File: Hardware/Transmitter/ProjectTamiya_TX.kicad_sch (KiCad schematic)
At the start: 40 parts, among them J1 Boot, J10 NRF, J2 Power, J3 Serial, J4 Steering, J5 Throttle, J6 ENC1, J7 OLED, J8 ENC2, J9 Debug, Q1 RYC002N05T316, Q2 RYC002N05T316, Q3 RYC002N05T316, SW1 Reset, SW2 Switch, U1 STM32F303CCT6, U2 AP2111H-3.3TRG1, Y1 LFXTAL063189 [15pF]

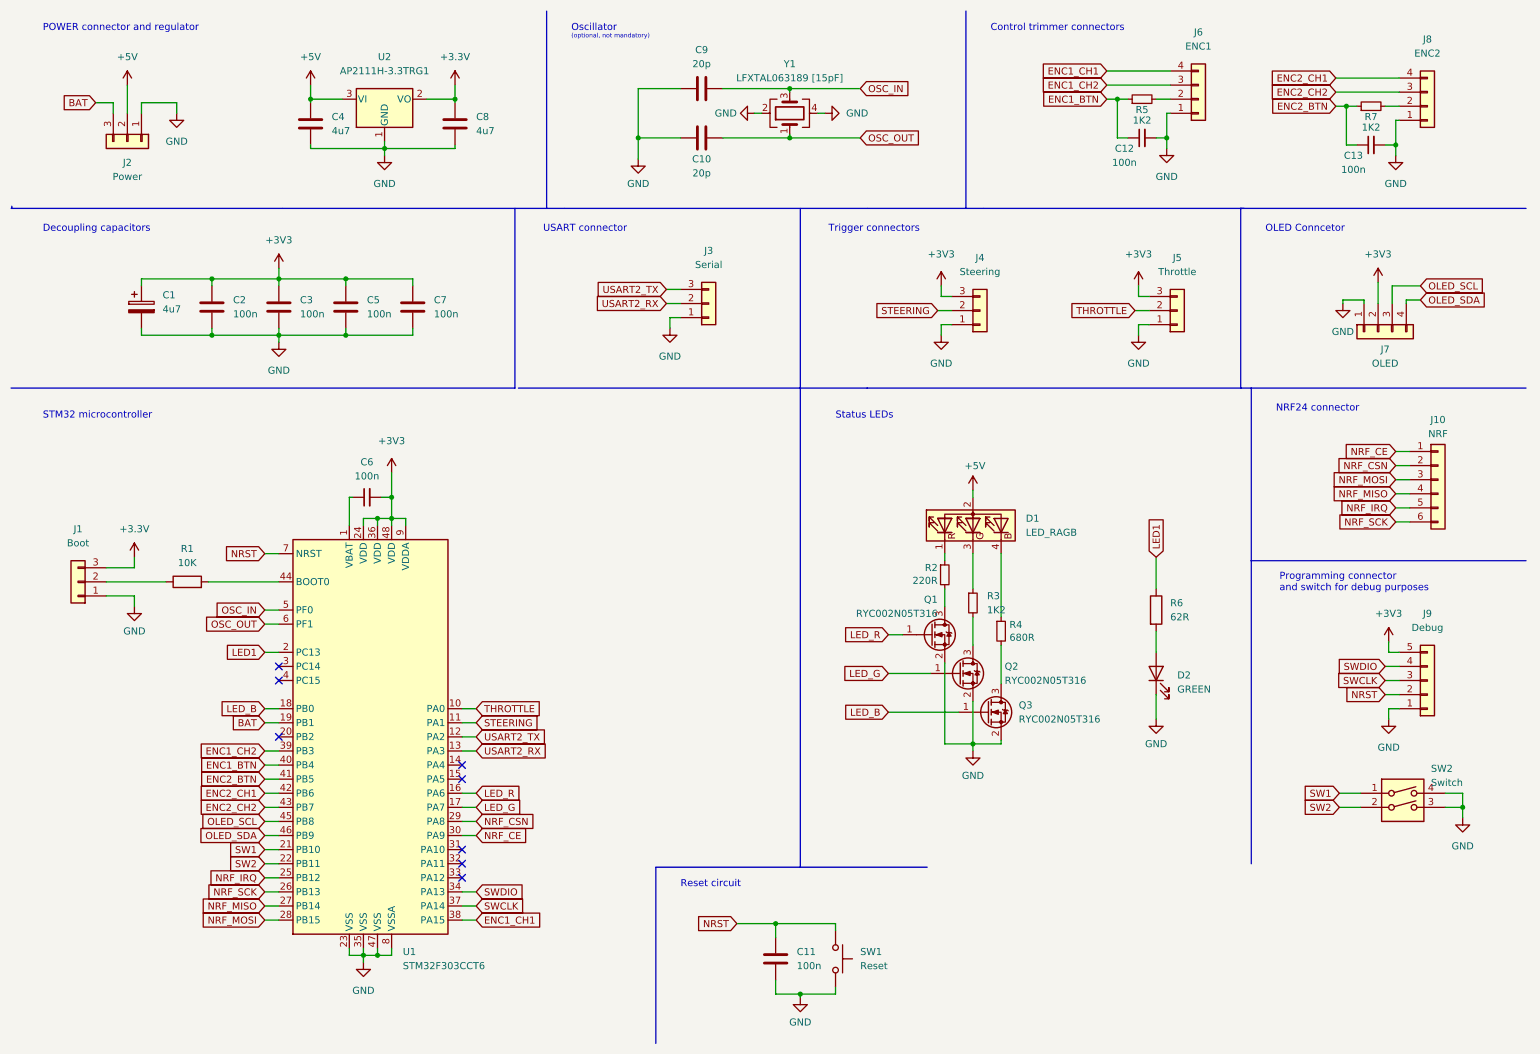
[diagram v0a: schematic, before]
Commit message: Small schematics adjustments
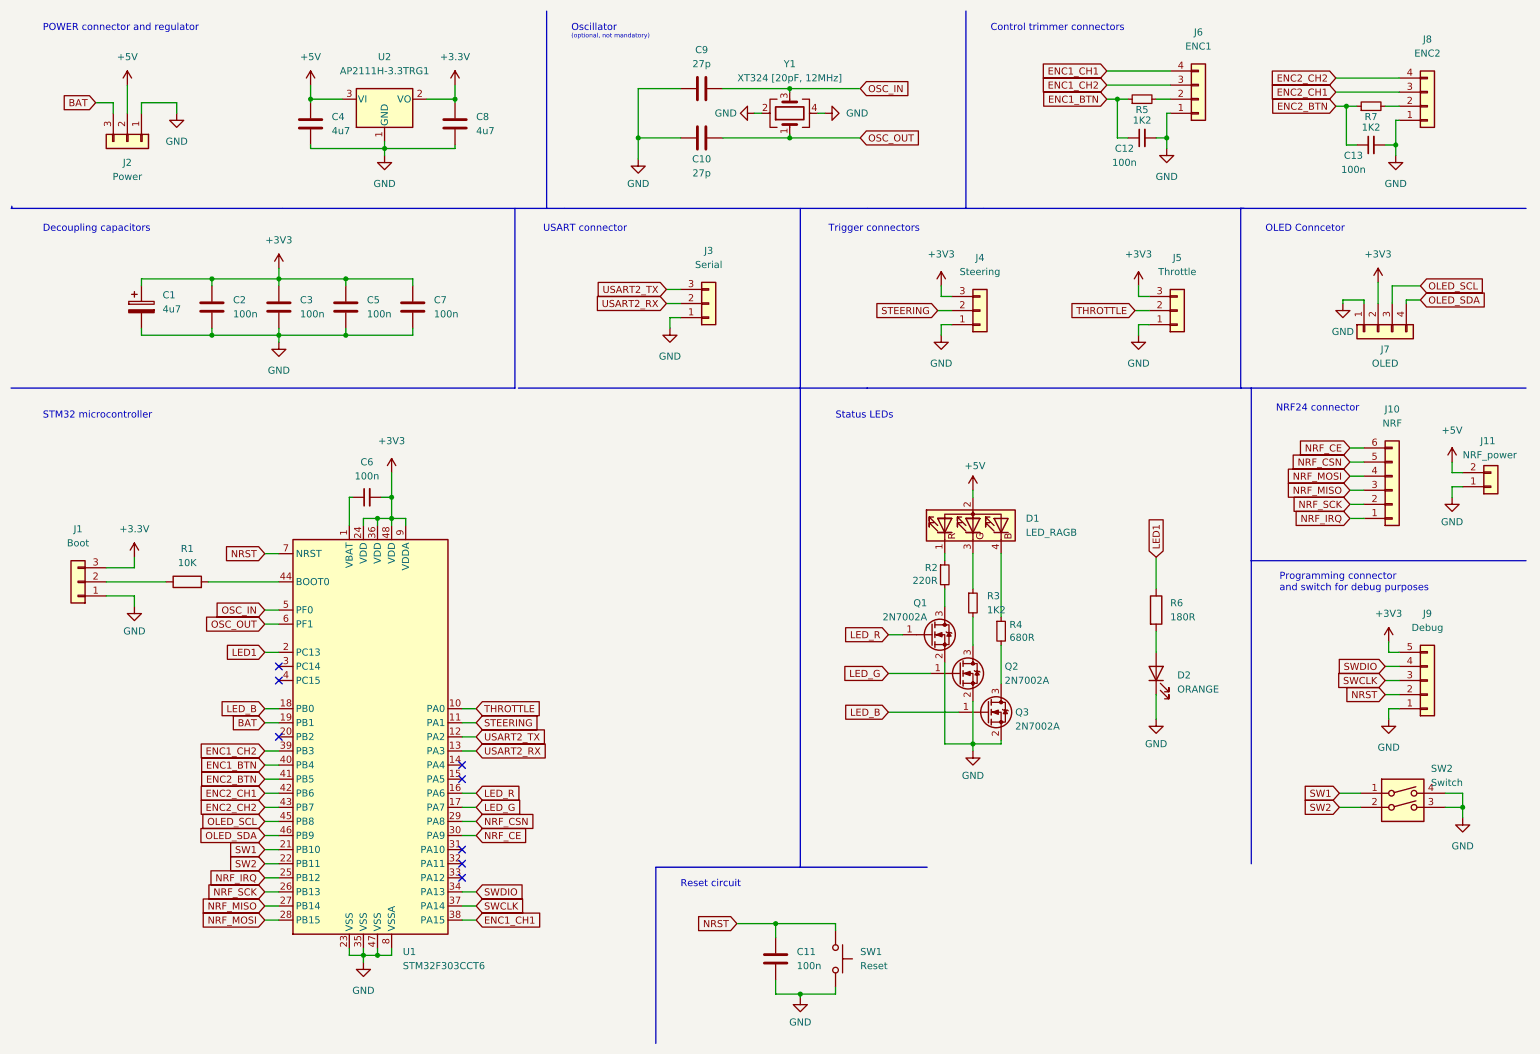
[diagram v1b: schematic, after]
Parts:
- removed Q1, Q2, Q3: RYC002N05T316, Package_TO_SOT_SMD:SOT-23, symbol Device:Q_NMOS_GSD
- added J11: NRF_power, Connector_Wire:SolderWire-0.25sqmm_1x02_P4.2mm_D0.65mm_OD1.7mm_Relief, symbol Connector_Generic:Conn_01x02
- added Q1, Q2, Q3: 2N7002A, Package_TO_SOT_SMD:SOT-23, symbol Transistor_FET:2N7002
- C10, C9: value 20p -> 27p
- D2: value GREEN -> ORANGE
- J10: footprint Connector_Wire:SolderWire-0.25sqmm_1x06_P4.2mm_D0.65mm_OD1.7mm_Relief -> Connector_Wire:SolderWire-0.15sqmm_1x06_P4mm_D0.5mm_OD1.5mm_Relief
- J7: footprint Connector_PinSocket_2.54mm:PinSocket_1x04_P2.54mm_Vertical -> Connector_PinSocket_2.54mm:PinSocket_1x04_P2.54mm_Vertical_SMD_Pin1Left
- R2, R3, R4: footprint Resistor_SMD:R_0603_1608Metric_Pad0.98x0.95mm_HandSolder -> Resistor_THT:R_Axial_DIN0204_L3.6mm_D1.6mm_P2.54mm_Vertical
- R6: value 62R -> 180R
- Y1: value LFXTAL063189 [15pF] -> XT324 [20pF, 12MHz]; footprint Crystal:Crystal_SMD_5032-4Pin_5.0x3.2mm -> Crystal:Crystal_SMD_3225-4Pin_3.2x2.5mm_HandSoldering
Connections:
- net +5V: now also J11.2 (Pin_2)
- net ENC2_CH1: now also J8.3 (Pin_3); no longer J8.4 (Pin_4)
- net ENC2_CH2: now also J8.4 (Pin_4); no longer J8.3 (Pin_3)
- net GND: now also J11.1 (Pin_1), Q1.2 (S), Q2.2 (S), Q3.2 (S)
- net LED_B: now also Q3.1 (G)
- net LED_G: now also Q2.1 (G)
- net LED_R: now also Q1.1 (G)
- net NRF_CE: now also J10.6 (Pin_6); no longer J10.1 (Pin_1)
- net NRF_CSN: now also J10.5 (Pin_5); no longer J10.2 (Pin_2)
- net NRF_IRQ: now also J10.1 (Pin_1); no longer J10.5 (Pin_5)
- net NRF_MISO: now also J10.3 (Pin_3); no longer J10.4 (Pin_4)
- net NRF_MOSI: now also J10.4 (Pin_4); no longer J10.3 (Pin_3)
- net NRF_SCK: now also J10.2 (Pin_2); no longer J10.6 (Pin_6)
- net at R3.2: now also Q2.3 (D)
- net at R4.2: now also Q3.3 (D)
- net at R2.2: now also Q1.3 (D)
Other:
- title: ProjectTamiya - Transmitter schematics -> ProjectTamiya - Transmitter
- moved on the sheet: J10

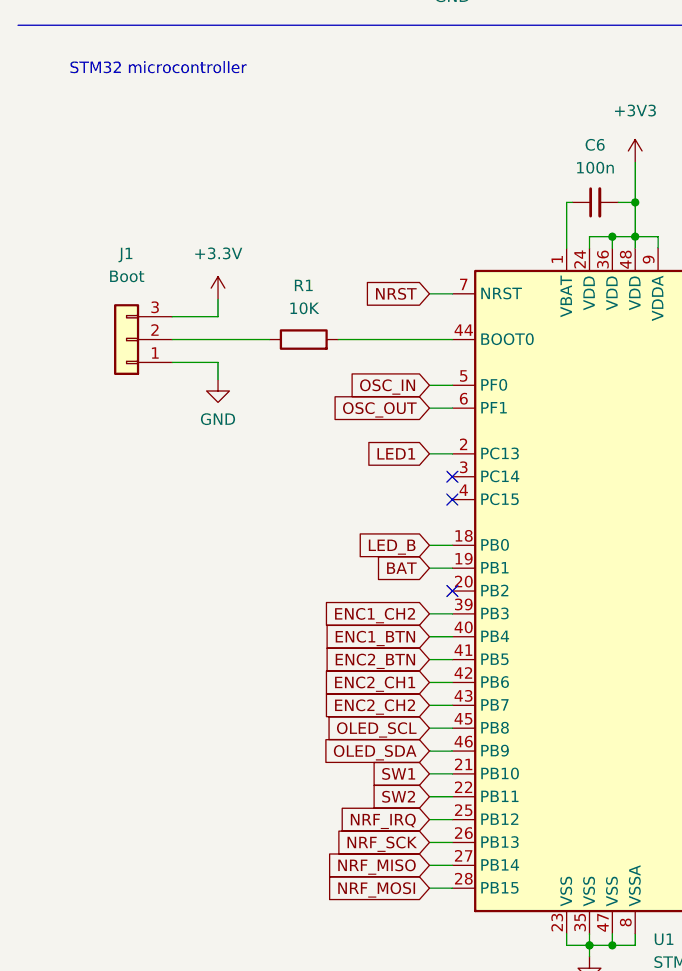
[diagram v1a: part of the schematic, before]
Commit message: Switch pin assignment change, updated schematics, complete PCB
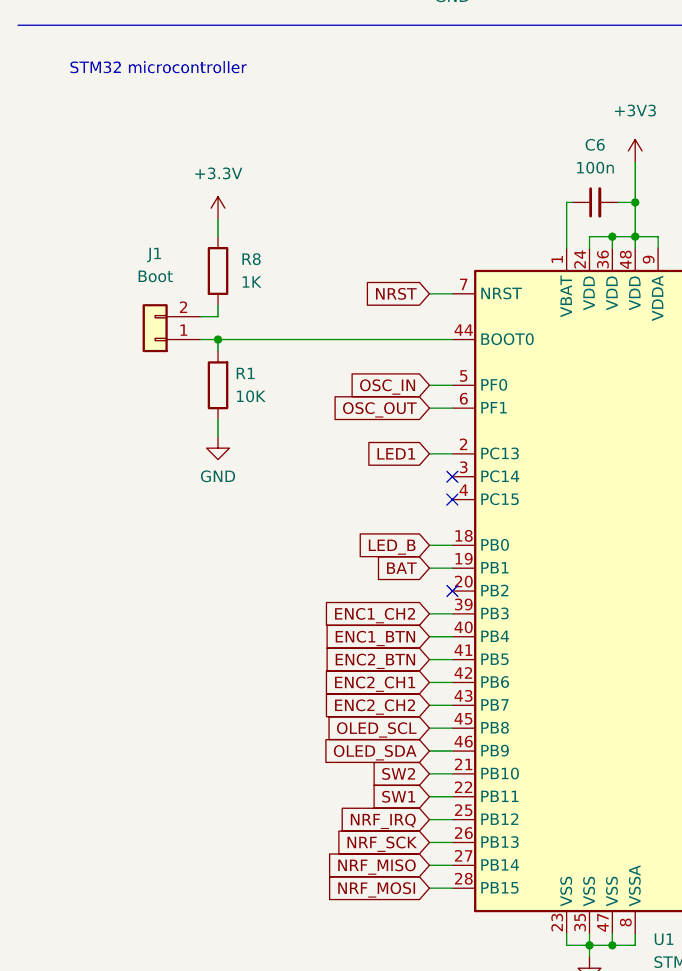
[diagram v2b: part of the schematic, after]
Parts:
- removed J1: Boot, Connector_PinHeader_2.54mm:PinHeader_1x03_P2.54mm_Vertical, symbol Connector_Generic:Conn_01x03
- added J1: Boot, Connector_PinHeader_2.54mm:PinHeader_1x02_P2.54mm_Vertical, symbol Connector_Generic:Conn_01x02
- added R8: 1K, Resistor_SMD:R_0603_1608Metric_Pad0.98x0.95mm_HandSolder, symbol Device:R
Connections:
- net +3V3: now also R8.1
- net GND: now also R1.1
- net SW1: now also U1.22 (PB11); no longer U1.21 (PB10)
- net SW2: now also U1.21 (PB10); no longer U1.22 (PB11)
- net at R1.2, U1.44 (BOOT0): now also J1.1 (Pin_1)
- new net: J1.2 (Pin_2), R8.2
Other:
- moved on the sheet: R1

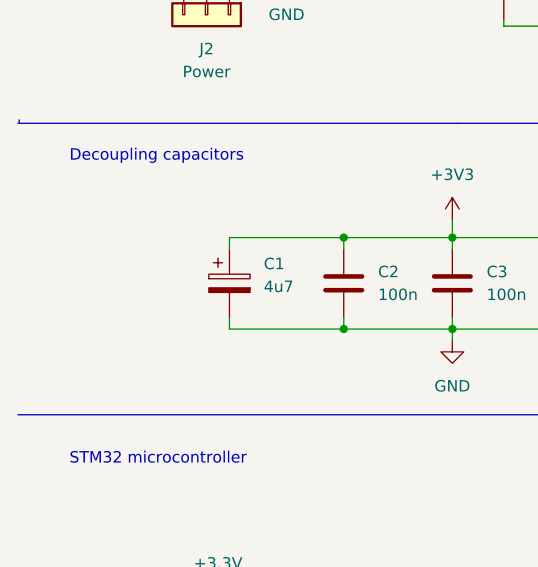
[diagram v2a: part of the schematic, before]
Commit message: Small PCB routing changes, silkscreen improvements
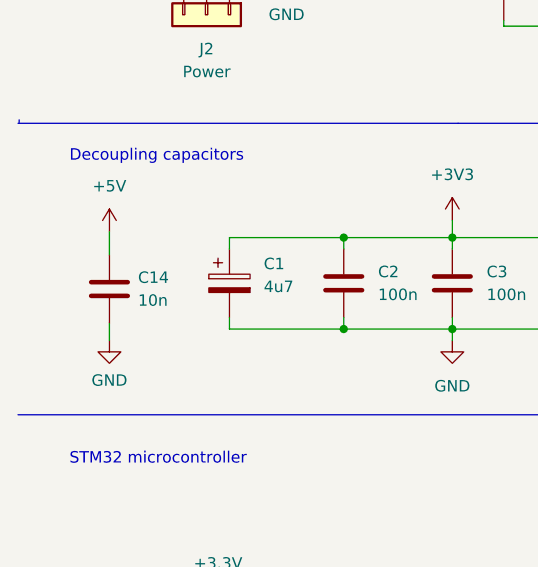
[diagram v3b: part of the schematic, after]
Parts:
- added C14: 10n, Capacitor_SMD:C_0603_1608Metric_Pad1.08x0.95mm_HandSolder, symbol Device:C
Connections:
- net +5V: now also C14.1
- net GND: now also C14.2
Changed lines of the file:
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@@
+    (stroke (width 0) (type default) (color 0 0 0 0))
+  )
+  (wire (pts (xy 22.225 69.85) (xy 22.225 71.755))
     (stroke (width 0) (type default) (color 0 0 0 0))
   )
@@
   )
   (wire (pts (xy 84.455 70.485) (xy 84.455 69.215))
+    (stroke (width 0) (type default) (color 0 0 0 0))
+  )
+  (wire (pts (xy 22.225 59.69) (xy 22.225 62.23))
     (stroke (width 0) (type default) (color 0 0 0 0))
   )
@@
     (pin "5")
   )
+  (symbol (lib_id "power:+5V") (at 22.225 59.69 0) (unit 1)
+    (in_bom yes) (on_board yes) (fields_autoplaced)
+    (property "Reference" "#PWR033" (id 0) (at 22.225 63.5 0)
+      (effects (font (size 1.27 1.27)) hide)
+    )
+    (property "Value" "+5V" (id 1) (at 22.225 54.61 0))
+    (property "Footprint" "" (id 2) (at 22.225 59.69 0)
+      (effects (font (size 1.27 1.27)) hide)
+    )
+    (property "Datasheet" "" (id 3) (at 22.225 59.69 0)
+      (effects (font (size 1.27 1.27)) hide)
+    )
+    (pin "1")
+  )
   (symbol (lib_id "Device:C") (at 60.325 65.405 0) (unit 1)
     (in_bom yes) (on_board yes) (fields_autoplaced)
@@
     (pin "1")
   )
+  (symbol (lib_id "Device:C") (at 22.225 66.04 0) (unit 1)
+    (in_bom yes) (on_board yes) (fields_autoplaced)
+    (property "Reference" "C14" (id 0) (at 25.4 64.7699 0)
+      (effects (font (size 1.27 1.27)) (justify left))
+    )
+    (property "Value" "10n" (id 1) (at 25.4 67.3099 0)
+      (effects (font (size 1.27 1.27)) (justify left))
+    )
+    (property "Footprint" "Capacitor_SMD:C_0603_1608Metric_Pad1.08x0.95mm_HandSolder" (id 2) (at 23.1902 69.85 0)
+      (effects (font (size 1.27 1.27)) hide)
+    )
+    (property "Datasheet" "~" (id 3) (at 22.225 66.04 0)
+      (effects (font (size 1.27 1.27)) hide)
+    )
+    (pin "1")
+    (pin "2")
+  )
   (symbol (lib_id "power:+3V3") (at 179.705 61.595 0) (unit 1)
     (in_bom yes) (on_board yes) (fields_autoplaced)
@@
     (pin "3")
     (pin "4")
+  )
+  (symbol (lib_id "power:GND") (at 22.225 71.755 0) (unit 1)
+    (in_bom yes) (on_board yes) (fields_autoplaced)
+    (property "Reference" "#PWR034" (id 0) (at 22.225 78.105 0)
+      (effects (font (size 1.27 1.27)) hide)
+    )
+    (property "Value" "GND" (id 1) (at 22.225 76.2 0))
+    (property "Footprint" "" (id 2) (at 22.225 71.755 0)
+      (effects (font (size 1.27 1.27)) hide)
+    )
+    (property "Datasheet" "" (id 3) (at 22.225 71.755 0)
+      (effects (font (size 1.27 1.27)) hide)
+    )
+    (pin "1")
   )
   (symbol (lib_id "power:+5V") (at 271.78 93.345 0) (unit 1)
@@
       (reference "#PWR032") (unit 1) (value "GND") (footprint "")
     )
+    (path "/b51343d5-5258-4bf6-a38b-315156655fe7"
+      (reference "#PWR033") (unit 1) (value "+5V") (footprint "")
+    )
+    (path "/fc2e6937-75ad-4c5e-862d-3bdf44129aa7"
+      (reference "#PWR034") (unit 1) (value "GND") (footprint "")
+    )
     (path "/4088a0a9-236b-4b9b-a260-6083e64fab90"
       (reference "C1") (unit 1) (value "4u7") (footprint "Capacitor_Tantalum_SMD:CP_EIA-1608-10_AVX-L_Pad1.25x1.05mm_HandSolder")
@@
       (reference "C13") (unit 1) (value "100n") (footprint "Capacitor_SMD:C_0603_1608Metric_Pad1.08x0.95mm_HandSolder")
     )
+    (path "/c3f4e4fd-33f7-404b-a4b5-b1fa76c627d6"
+      (reference "C14") (unit 1) (value "10n") (footprint "Capacitor_SMD:C_0603_1608Metric_Pad1.08x0.95mm_HandSolder")
+    )
     (path "/9a0eb21d-73ee-4fea-bf1f-59fce775cdc8"

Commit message: Final checkup and small adjustments
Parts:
- Q1, Q2, Q3: value 2N7002A -> 2N7002BK
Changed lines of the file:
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@@
       (effects (font (size 1.27 1.27)) (justify left))
     )
-    (property "Value" "2N7002A" (id 1) (at 191.135 132.715 0)
+    (property "Value" "2N7002BK" (id 1) (at 191.135 132.715 0)
       (effects (font (size 1.27 1.27)) (justify left))
     )
@@
       (effects (font (size 1.27 1.27)) (justify right))
     )
-    (property "Value" "2N7002A" (id 1) (at 177.165 121.285 0)
+    (property "Value" "2N7002BK" (id 1) (at 177.165 121.285 0)
       (effects (font (size 1.27 1.27)) (justify right))
     )
@@
       (effects (font (size 1.27 1.27)) (justify left))
     )
-    (property "Value" "2N7002A" (id 1) (at 193.04 140.97 0)
+    (property "Value" "2N7002BK" (id 1) (at 193.04 140.97 0)
       (effects (font (size 1.27 1.27)) (justify left))
     )
@@
     )
     (path "/4a4d9b9b-c50f-4ef0-8277-cdd97ceed0a6"
-      (reference "Q1") (unit 1) (value "2N7002A") (footprint "Package_TO_SOT_SMD:SOT-23")
+      (reference "Q1") (unit 1) (value "2N7002BK") (footprint "Package_TO_SOT_SMD:SOT-23")
     )
     (path "/2bb276a7-8ab2-4be3-9b32-a7ea311015c9"
-      (reference "Q2") (unit 1) (value "2N7002A") (footprint "Package_TO_SOT_SMD:SOT-23")
+      (reference "Q2") (unit 1) (value "2N7002BK") (footprint "Package_TO_SOT_SMD:SOT-23")
     )
     (path "/9cd35799-ec18-4e90-9608-c6514838a377"
-      (reference "Q3") (unit 1) (value "2N7002A") (footprint "Package_TO_SOT_SMD:SOT-23")
+      (reference "Q3") (unit 1) (value "2N7002BK") (footprint "Package_TO_SOT_SMD:SOT-23")
     )
     (path "/ab73a559-2422-46c8-acb5-de8dbb2705dd"
